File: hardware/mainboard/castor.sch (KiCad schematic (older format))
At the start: 41 parts, among them Q1 MMBT3904, U3 TL074, U4 74LVC2G74, U5 MCP6001-OT, U6 TL074

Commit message: Fix incorrect MPN for 10uF cap
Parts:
- C11, C12, C13: mpn MF-CAP-1206-10uF -> (none); mpn alt GRT31CR61H106ME01L -> GRM21BR61E106KA73K
- C6, C9: mpn alt (none) -> GRM21BR61E106KA73K
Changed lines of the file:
@@
 F 6 "C0603C472F5GACTU" H 2350 1250 50  0001 C CNN "mpn"
 F 7 "1%, 50v" H 2350 1250 50  0001 C CNN "mpn specs"
+F 8 "GRM21BR61E106KA73K" H 2350 1250 50  0001 C CNN "mpn alt"
 	1    2350 1250
 	0    1    1    0
@@
 F 6 "C0603C472F5GACTU" H 3300 2500 50  0001 C CNN "mpn"
 F 7 "1% 50v" H 3300 2500 50  0001 C CNN "mpn specs"
+F 8 "GRM21BR61E106KA73K" H 3300 2500 50  0001 C CNN "mpn alt"
 	1    3300 2500
 	0    1    1    0
@@
 F 3 "~" H 7950 1550 50  0001 C CNN
 F 4 "yes" H 7950 1550 50  0001 C CNN "finalized"
-F 5 "MF-CAP-1206-10uF" H 7950 1550 50  0001 C CNN "mpn"
+F 5 "" H 7950 1550 50  0001 C CNN "mpn"
 F 6 "10% 16v" H 7950 1550 50  0001 C CNN "mpn specs"
-F 7 "GRT31CR61H106ME01L" H 7950 1550 50  0001 C CNN "mpn alt"
+F 7 "GRM21BR61E106KA73K" H 7950 1550 50  0001 C CNN "mpn alt"
 	1    7950 1550
 	0    1    1    0
@@
 F 3 "~" H 7950 2700 50  0001 C CNN
 F 4 "yes" H 7950 2700 50  0001 C CNN "finalized"
-F 5 "MF-CAP-1206-10uF" H 7950 2700 50  0001 C CNN "mpn"
+F 5 "" H 7950 2700 50  0001 C CNN "mpn"
 F 6 "10% 16v" H 7950 2700 50  0001 C CNN "mpn specs"
-F 7 "GRT31CR61H106ME01L" H 7950 2700 50  0001 C CNN "mpn alt"
+F 7 "GRM21BR61E106KA73K" H 7950 2700 50  0001 C CNN "mpn alt"
 	1    7950 2700
 	0    1    1    0
@@
 F 3 "~" H 7950 3850 50  0001 C CNN
 F 4 "yes" H 7950 3850 50  0001 C CNN "finalized"
-F 5 "MF-CAP-1206-10uF" H 7950 3850 50  0001 C CNN "mpn"
+F 5 "" H 7950 3850 50  0001 C CNN "mpn"
 F 6 "10% 16v" H 7950 3850 50  0001 C CNN "mpn specs"
-F 7 "GRT31CR61H106ME01L" H 7950 3850 50  0001 C CNN "mpn alt"
+F 7 "GRM21BR61E106KA73K" H 7950 3850 50  0001 C CNN "mpn alt"
 	1    7950 3850
 	0    1    1    0

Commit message: Fix a few more mpns
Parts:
- C10, C5, C7, C8: mpn alt GRM188R72A104KA35D -> GCM188R91E104KA37D
- C11, C12, C13: mpn (none) -> GRM21BR61E106KA73K; mpn alt GRM21BR61E106KA73K -> (none)
- C14, C15, C16: mpn alt GCM1885C2A220JA16D -> GCM1885C2A220JA16J
- C6: mpn alt GRM21BR61E106KA73K -> (none)
- C9: mpn alt GRM21BR61E106KA73K -> (none); mpn specs 1% 50v -> 1%, 50v
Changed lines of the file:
@@
 F 6 "C0603C472F5GACTU" H 2350 1250 50  0001 C CNN "mpn"
 F 7 "1%, 50v" H 2350 1250 50  0001 C CNN "mpn specs"
-F 8 "GRM21BR61E106KA73K" H 2350 1250 50  0001 C CNN "mpn alt"
+F 8 "" H 2350 1250 50  0001 C CNN "mpn alt"
 	1    2350 1250
 	0    1    1    0
@@
 F 5 "yes" H 3300 2500 50  0001 C CNN "finalized"
 F 6 "C0603C472F5GACTU" H 3300 2500 50  0001 C CNN "mpn"
-F 7 "1% 50v" H 3300 2500 50  0001 C CNN "mpn specs"
-F 8 "GRM21BR61E106KA73K" H 3300 2500 50  0001 C CNN "mpn alt"
+F 7 "1%, 50v" H 3300 2500 50  0001 C CNN "mpn specs"
+F 8 "" H 3300 2500 50  0001 C CNN "mpn alt"
 	1    3300 2500
 	0    1    1    0
@@
 F 3 "~" H 7950 1550 50  0001 C CNN
 F 4 "yes" H 7950 1550 50  0001 C CNN "finalized"
-F 5 "" H 7950 1550 50  0001 C CNN "mpn"
+F 5 "GRM21BR61E106KA73K" H 7950 1550 50  0001 C CNN "mpn"
 F 6 "10% 16v" H 7950 1550 50  0001 C CNN "mpn specs"
-F 7 "GRM21BR61E106KA73K" H 7950 1550 50  0001 C CNN "mpn alt"
+F 7 "" H 7950 1550 50  0001 C CNN "mpn alt"
 	1    7950 1550
 	0    1    1    0
@@
 F 5 "MF-CAP-0603-22pF" H 8850 1000 50  0001 C CNN "mpn"
 F 6 "5% 100v" H 8850 1000 50  0001 C CNN "mpn specs"
-F 7 "GCM1885C2A220JA16D" H 8850 1000 50  0001 C CNN "mpn alt"
+F 7 "GCM1885C2A220JA16J" H 8850 1000 50  0001 C CNN "mpn alt"
 	1    8850 1000
 	0    1    1    0
@@
 F 3 "~" H 7950 2700 50  0001 C CNN
 F 4 "yes" H 7950 2700 50  0001 C CNN "finalized"
-F 5 "" H 7950 2700 50  0001 C CNN "mpn"
+F 5 "GRM21BR61E106KA73K" H 7950 2700 50  0001 C CNN "mpn"
 F 6 "10% 16v" H 7950 2700 50  0001 C CNN "mpn specs"
-F 7 "GRM21BR61E106KA73K" H 7950 2700 50  0001 C CNN "mpn alt"
+F 7 "" H 7950 2700 50  0001 C CNN "mpn alt"
 	1    7950 2700
 	0    1    1    0
@@
 F 5 "MF-CAP-0603-22pF" H 8850 2150 50  0001 C CNN "mpn"
 F 6 "5% 100v" H 8850 2150 50  0001 C CNN "mpn specs"
-F 7 "GCM1885C2A220JA16D" H 8850 2150 50  0001 C CNN "mpn alt"
+F 7 "GCM1885C2A220JA16J" H 8850 2150 50  0001 C CNN "mpn alt"
 	1    8850 2150
 	0    1    1    0
@@
 F 5 "MF-CAP-0603-0.1uF" H 3450 6850 50  0001 C CNN "mpn"
 F 6 "10%, 25v" H 3450 6850 50  0001 C CNN "mpn specs"
-F 7 "GRM188R72A104KA35D" H 3450 6850 50  0001 C CNN "mpn alt"
+F 7 "GCM188R91E104KA37D" H 3450 6850 50  0001 C CNN "mpn alt"
 	1    3450 6850
 	1    0    0    -1
@@
 F 5 "MF-CAP-0603-0.1uF" H 3000 6850 50  0001 C CNN "mpn"
 F 6 "10%, 25v" H 3000 6850 50  0001 C CNN "mpn specs"
-F 7 "GRM188R72A104KA35D" H 3000 6850 50  0001 C CNN "mpn alt"
+F 7 "GCM188R91E104KA37D" H 3000 6850 50  0001 C CNN "mpn alt"
 	1    3000 6850
 	1    0    0    -1
@@
 F 5 "MF-CAP-0603-0.1uF" H 2550 6850 50  0001 C CNN "mpn"
 F 6 "10%, 25v" H 2550 6850 50  0001 C CNN "mpn specs"
-F 7 "GRM188R72A104KA35D" H 2550 6850 50  0001 C CNN "mpn alt"
+F 7 "GCM188R91E104KA37D" H 2550 6850 50  0001 C CNN "mpn alt"
 	1    2550 6850
 	1    0    0    -1
@@
 F 5 "MF-CAP-0603-0.1uF" H 2100 6850 50  0001 C CNN "mpn"
 F 6 "10%, 25v" H 2100 6850 50  0001 C CNN "mpn specs"
-F 7 "GRM188R72A104KA35D" H 2100 6850 50  0001 C CNN "mpn alt"
+F 7 "GCM188R91E104KA37D" H 2100 6850 50  0001 C CNN "mpn alt"
 	1    2100 6850
 	1    0    0    -1
@@
 F 5 "MF-CAP-0603-22pF" H 8850 3300 50  0001 C CNN "mpn"
 F 6 "5% 100v" H 8850 3300 50  0001 C CNN "mpn specs"
-F 7 "GCM1885C2A220JA16D" H 8850 3300 50  0001 C CNN "mpn alt"
+F 7 "GCM1885C2A220JA16J" H 8850 3300 50  0001 C CNN "mpn alt"
 	1    8850 3300
 	0    1    1    0
@@
 F 3 "~" H 7950 3850 50  0001 C CNN
 F 4 "yes" H 7950 3850 50  0001 C CNN "finalized"
-F 5 "" H 7950 3850 50  0001 C CNN "mpn"
+F 5 "GRM21BR61E106KA73K" H 7950 3850 50  0001 C CNN "mpn"
 F 6 "10% 16v" H 7950 3850 50  0001 C CNN "mpn specs"
-F 7 "GRM21BR61E106KA73K" H 7950 3850 50  0001 C CNN "mpn alt"
+F 7 "" H 7950 3850 50  0001 C CNN "mpn alt"
 	1    7950 3850
 	0    1    1    0

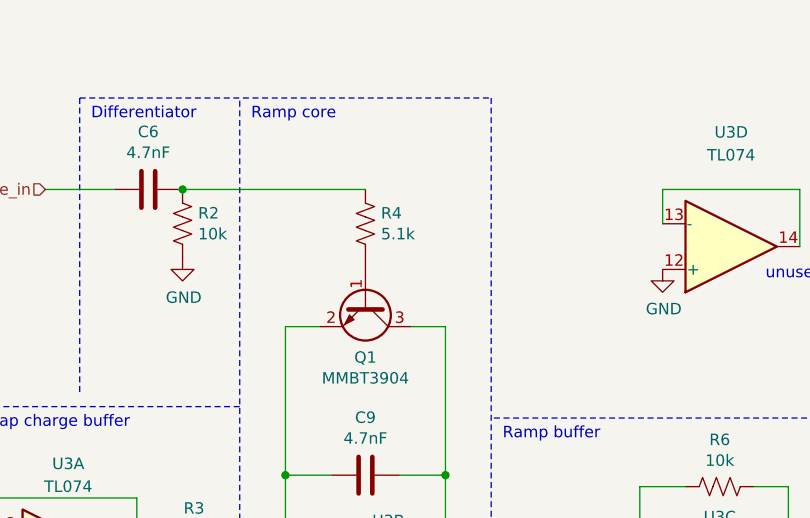
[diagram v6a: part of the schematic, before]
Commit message: Update R4, R28 to 2.2k
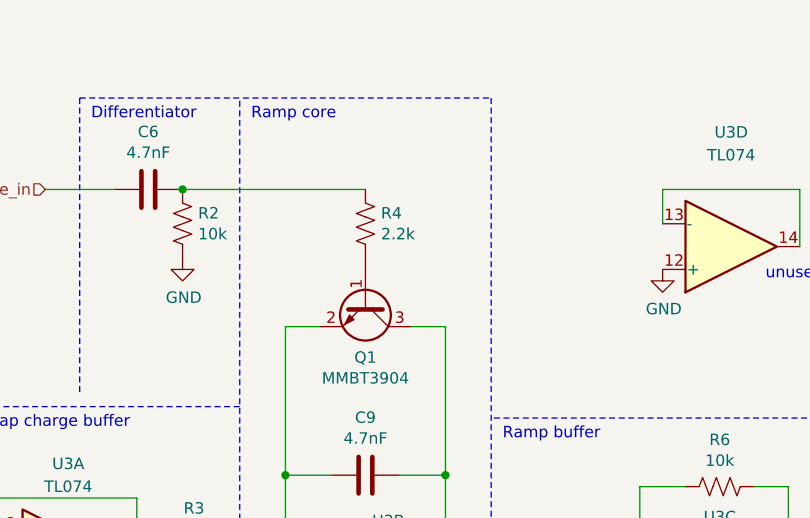
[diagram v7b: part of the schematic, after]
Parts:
- R4: value 5.1k -> 2.2k
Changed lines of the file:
@@
 AR Path="/5F0E55E2/5EE54BED" Ref="R28"  Part="1"
 F 0 "R4" H 3232 1354 50  0000 R CNN
-F 1 "5.1k" H 3232 1445 50  0000 R CNN
+F 1 "2.2k" H 3232 1445 50  0000 R CNN
 F 2 "Resistor_SMD:R_0603_1608Metric_Pad1.05x0.95mm_HandSolder" V 3340 1390 50  0001 C CNN
 F 3 "~" H 3300 1400 50  0001 C CNN

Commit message: Change the RC differentiator capacitor to allow longer for discharging
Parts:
- C6, C9: mpn alt (none) -> C0603C472F3GECTU
- R4: mpn ERA-3AED512V -> ERA-3AED222V
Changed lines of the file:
@@
 F 6 "C0603C472F5GACTU" H 2350 1250 50  0001 C CNN "mpn"
 F 7 "1%, 50v" H 2350 1250 50  0001 C CNN "mpn specs"
-F 8 "" H 2350 1250 50  0001 C CNN "mpn alt"
+F 8 "C0603C472F3GECTU" H 2350 1250 50  0001 C CNN "mpn alt"
 	1    2350 1250
 	0    1    1    0
@@
 F 3 "~" H 3300 1400 50  0001 C CNN
 F 4 "yes" H 3300 1400 50  0001 C CNN "finalized"
-F 5 "ERA-3AED512V" H 3300 1400 50  0001 C CNN "mpn"
+F 5 "ERA-3AED222V" H 3300 1400 50  0001 C CNN "mpn"
 F 6 "100mW" H 3300 1400 50  0001 C CNN "mpn specs"
 	1    3300 1400
@@
 F 6 "C0603C472F5GACTU" H 3300 2500 50  0001 C CNN "mpn"
 F 7 "1%, 50v" H 3300 2500 50  0001 C CNN "mpn specs"
-F 8 "" H 3300 2500 50  0001 C CNN "mpn alt"
+F 8 "C0603C472F3GECTU" H 3300 2500 50  0001 C CNN "mpn alt"
 	1    3300 2500
 	0    1    1    0
